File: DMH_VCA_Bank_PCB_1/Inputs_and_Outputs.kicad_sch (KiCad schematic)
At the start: 30 parts, among them J0 Conn_01x01, J1 TS_Jack_6.35mm_Sw, J10 TS_Jack_6.35mm_Sw, J11 TS_Jack_6.35mm_Sw, J12 TS_Jack_6.35mm_Sw, J2 TS_Jack_6.35mm_Sw, J200 IDC_02x08, J3 TS_Jack_6.35mm_Sw, J4 TS_Jack_6.35mm_Sw, J5 TS_Jack_6.35mm_Sw, J50 Conn_01x06, J51 Conn_01x06, J52 Conn_01x06, J53 Conn_01x06, J6 TS_Jack_6.35mm_Sw, J7 TS_Jack_6.35mm_Sw, J8 TS_Jack_6.35mm_Sw, J9 TS_Jack_6.35mm_Sw

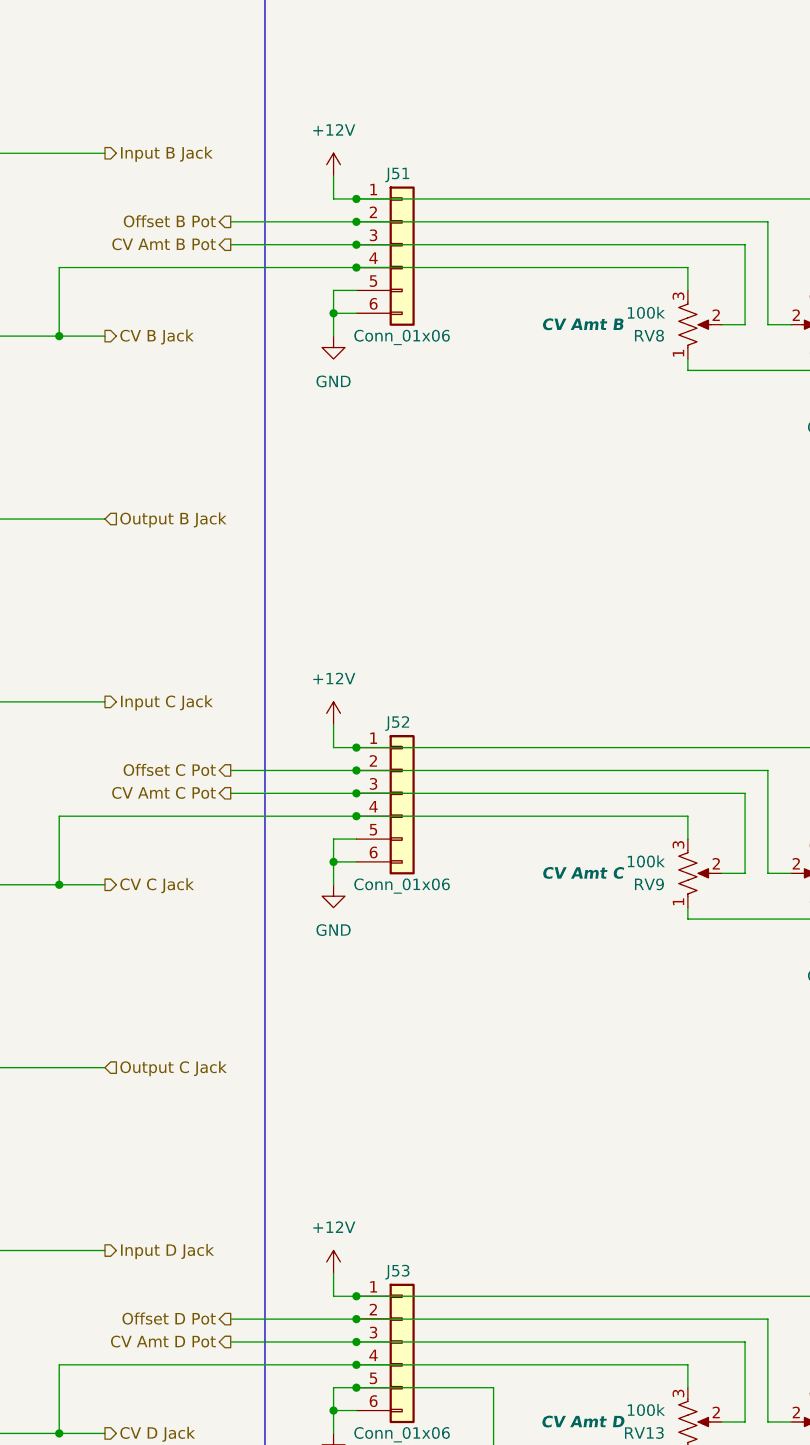
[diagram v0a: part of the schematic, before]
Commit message: Finished schematic of PCB 2
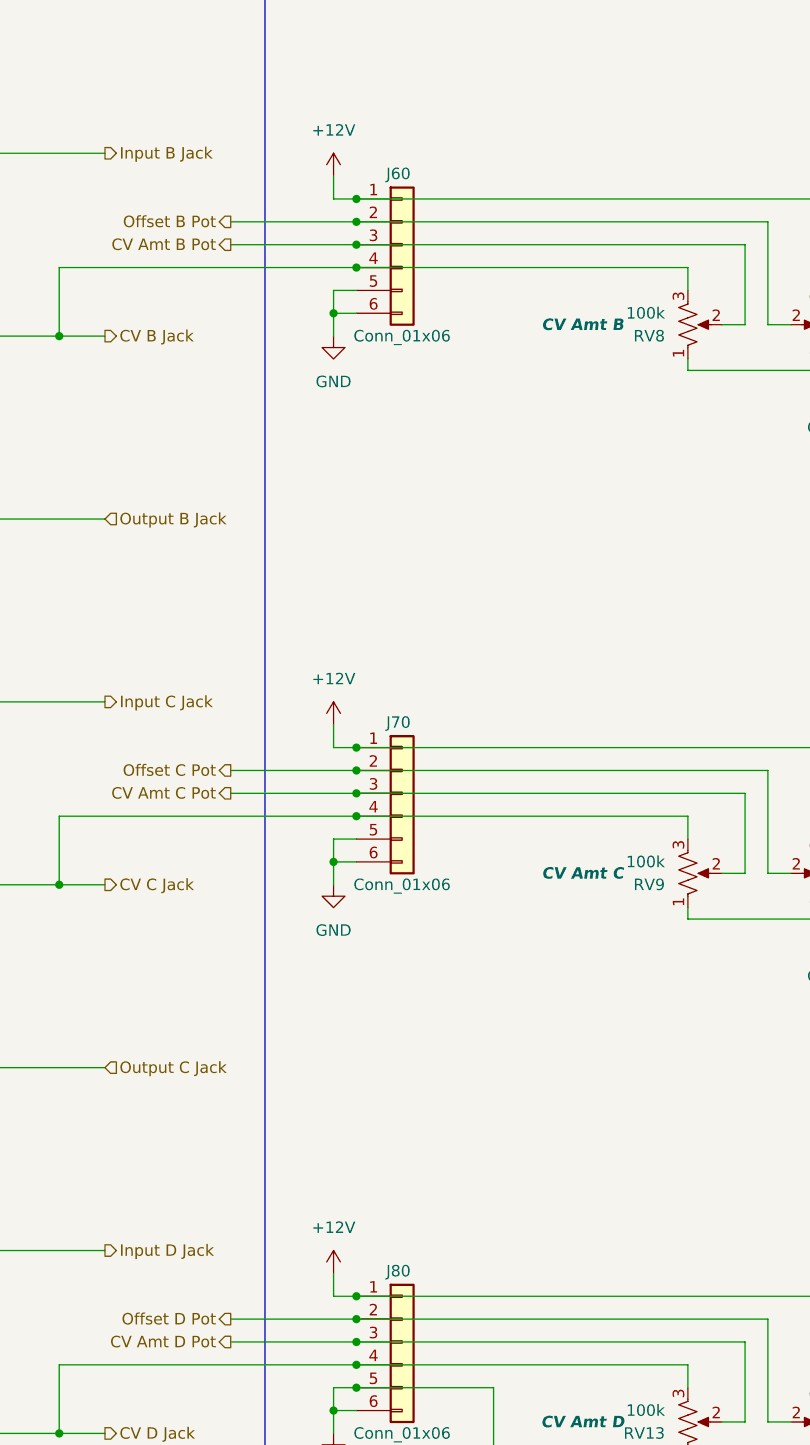
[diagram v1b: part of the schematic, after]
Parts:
- J50: footprint Connector_PinSocket_2.54mm:PinSocket_1x08_P2.54mm_Vertical -> Connector_PinHeader_2.54mm:PinHeader_1x06_P2.54mm_Vertical
- J60: renamed from J51; footprint Connector_PinSocket_2.54mm:PinSocket_1x08_P2.54mm_Vertical -> Connector_PinHeader_2.54mm:PinHeader_1x06_P2.54mm_Vertical
- J70: renamed from J52; footprint Connector_PinSocket_2.54mm:PinSocket_1x08_P2.54mm_Vertical -> Connector_PinHeader_2.54mm:PinHeader_1x06_P2.54mm_Vertical
- J80: renamed from J53; footprint Connector_PinSocket_2.54mm:PinSocket_1x08_P2.54mm_Vertical -> Connector_PinHeader_2.54mm:PinHeader_1x06_P2.54mm_Vertical
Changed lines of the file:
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@@
 		(on_board yes)
 		(dnp no)
-		(property "Reference" "J51"
+		(property "Reference" "J60"
 			(at 125.222 87.376 0)
 			(effects
@@
 			)
 		)
-		(property "Footprint" "Connector_PinSocket_2.54mm:PinSocket_1x08_P2.54mm_Vertical"
+		(property "Footprint" "Connector_PinHeader_2.54mm:PinHeader_1x06_P2.54mm_Vertical"
 			(at 127 95.25 0)
 			(effects
@@
 			(project "DMH_VCA_Bank_PCB_1"
 				(path "/58f4306d-5387-4983-bb08-41a2313fd315/ce3fef8b-9f1d-4178-b50b-4a046c030679"
-					(reference "J51")
+					(reference "J60")
 					(unit 1)
 				)
@@
 			)
 		)
-		(property "Footprint" "Connector_PinSocket_2.54mm:PinSocket_1x08_P2.54mm_Vertical"
+		(property "Footprint" "Connector_PinHeader_2.54mm:PinHeader_1x06_P2.54mm_Vertical"
 			(at 127 34.29 0)
 			(effects
@@
 		(on_board yes)
 		(dnp no)
-		(property "Reference" "J52"
+		(property "Reference" "J70"
 			(at 125.222 148.336 0)
 			(effects
@@
 			)
 		)
-		(property "Footprint" "Connector_PinSocket_2.54mm:PinSocket_1x08_P2.54mm_Vertical"
+		(property "Footprint" "Connector_PinHeader_2.54mm:PinHeader_1x06_P2.54mm_Vertical"
 			(at 127 156.21 0)
 			(effects
@@
 			(project "DMH_VCA_Bank_PCB_1"
 				(path "/58f4306d-5387-4983-bb08-41a2313fd315/ce3fef8b-9f1d-4178-b50b-4a046c030679"
-					(reference "J52")
+					(reference "J70")
 					(unit 1)
 				)
@@
 		(on_board yes)
 		(dnp no)
-		(property "Reference" "J53"
+		(property "Reference" "J80"
 			(at 125.222 209.296 0)
 			(effects
@@
 			)
 		)
-		(property "Footprint" "Connector_PinSocket_2.54mm:PinSocket_1x08_P2.54mm_Vertical"
+		(property "Footprint" "Connector_PinHeader_2.54mm:PinHeader_1x06_P2.54mm_Vertical"
 			(at 127 217.17 0)
 			(effects
@@
 			(project "DMH_VCA_Bank_PCB_1"
 				(path "/58f4306d-5387-4983-bb08-41a2313fd315/ce3fef8b-9f1d-4178-b50b-4a046c030679"
-					(reference "J53")
-					(unit 1)
-				)
+					(reference "J80")
+					(unit 1)
+				)
